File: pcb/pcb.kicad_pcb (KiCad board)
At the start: 4 copper layers, 88.3 x 88.4 mm, 32 parts, among them J1 USB_C_Receptacle_PowerOnly_6P, J10 Screw_Terminal_01x03, J2 Conn_01x04_Pin, J3 Screw_Terminal_01x03, J4 Screw_Terminal_01x04, J5 Screw_Terminal_01x02, J6 Screw_Terminal_01x02, J7 Screw_Terminal_01x04, J8 Screw_Terminal_01x07, J9 Screw_Terminal_01x02, K1 SANYOU_SRD_Form_A, Q1 2N2222A, Q2 AO3400A, U1 AMS1117-3.3, U2 ESP32-C6-MINI-1, U3 AM2302

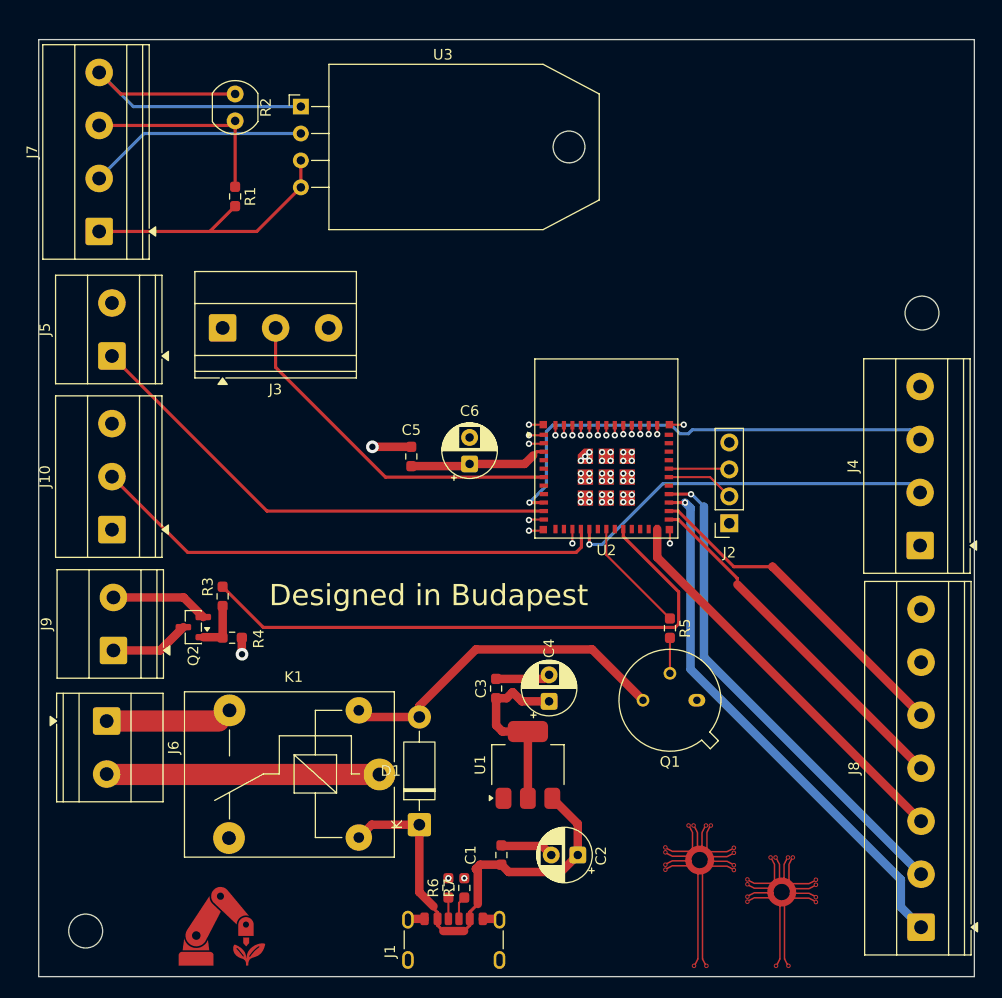
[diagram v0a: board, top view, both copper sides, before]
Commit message: fixing the layout
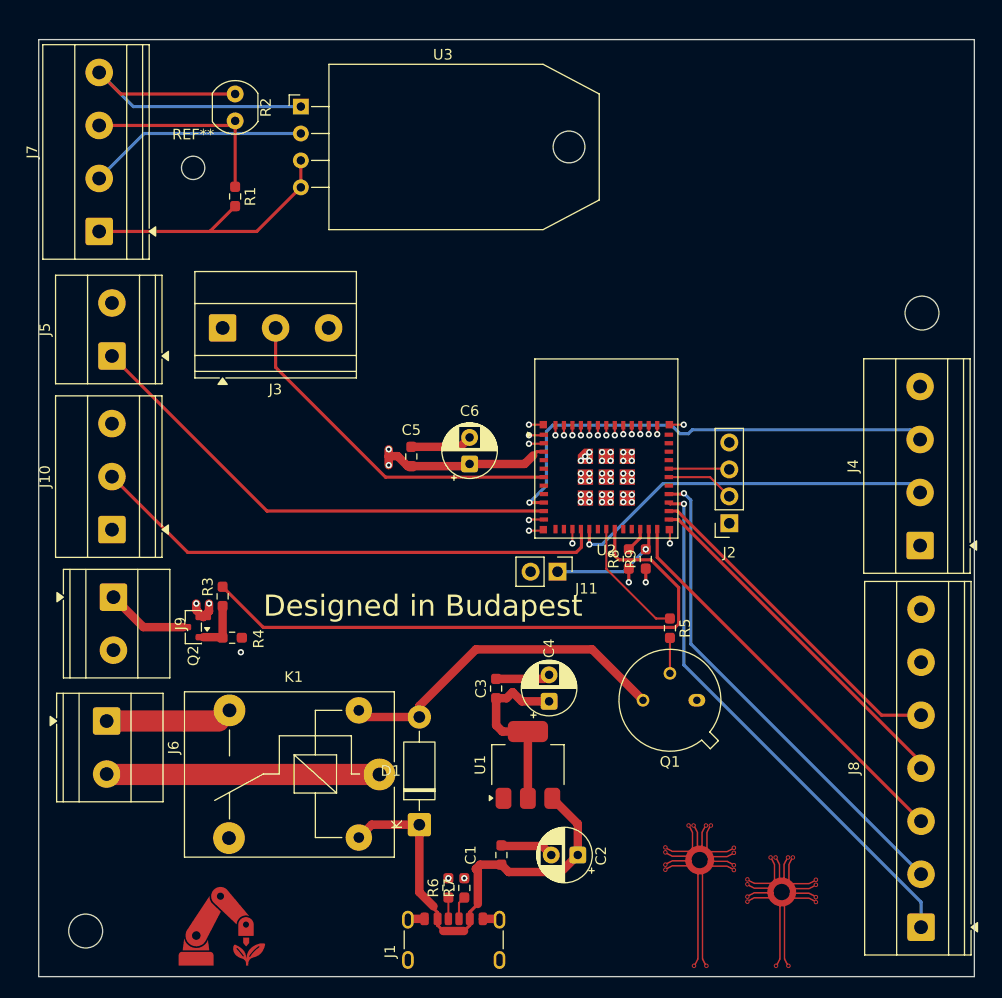
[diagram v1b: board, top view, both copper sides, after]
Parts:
- added J11: Conn_01x02_Pin, Connector_PinHeader_2.54mm:PinHeader_1x02_P2.54mm_Vertical, F.Cu at (113.4, 91.2)
- added R8: 10k, Resistor_SMD:R_0603_1608Metric_Pad0.98x0.95mm_HandSolder, F.Cu at (120.1, 90.0)
- added R9: 10k, Resistor_SMD:R_0603_1608Metric_Pad0.98x0.95mm_HandSolder, F.Cu at (121.7, 90.0)
- added REF**: MountingHole_2.2mm_M2, MountingHole:MountingHole_2.2mm_M2, F.Cu at (79.0, 53.1)
- moved J9 5.03 mm to (71.5, 93.6), turned to -90 degrees
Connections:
- U2 pad 19: unconnected-(U2-IO14-Pad19) -> /led_control/LED_control
- U2 pad 20: /led_control/LED_control -> unconnected-(U2-IO15-Pad20)
- U2 pad 22: unconnected-(U2-IO8-Pad22) -> /control/pullup for G8
- U2 pad 23: unconnected-(U2-IO9-Pad23) -> /control/input for G9
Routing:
- net /control/input for G9: track 0.00 -> 11.2 mm, vias 0 -> 1
- net +3.3V: track 31.0 -> 37.6 mm, vias 0 -> 4
- net GND: track 51.6 -> 46.6 mm, vias 61 -> 62
- net /screen/cs: track 49.3 -> 46.7 mm
- net /control/pullup for G8: track 0.00 -> 2.36 mm
- net /led_control/LED_control: track 55.9 -> 58.0 mm
- net /Pump control/PUMP_control: track 10.9 -> 11.7 mm

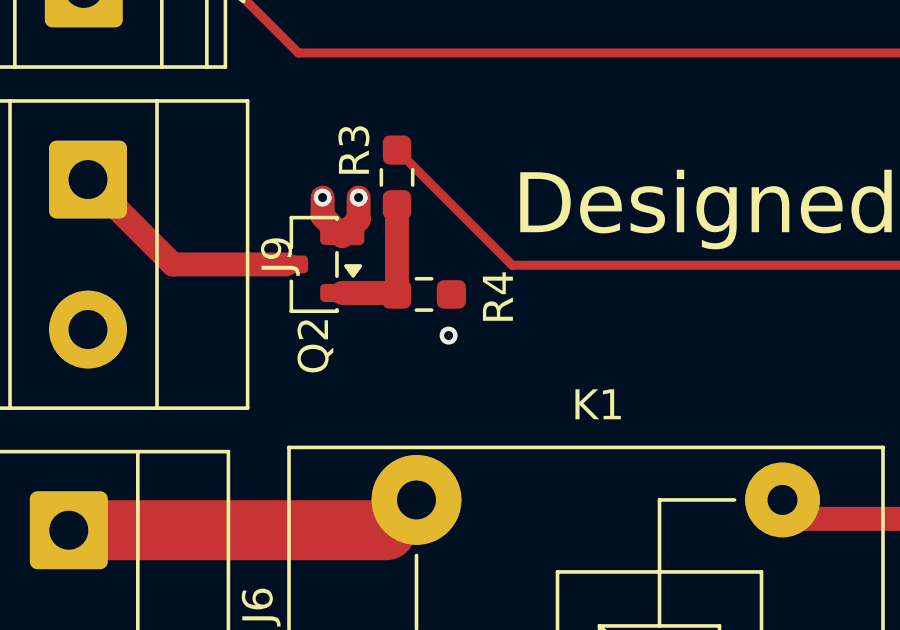
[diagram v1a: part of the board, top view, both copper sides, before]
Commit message: fixing the wireing mistake
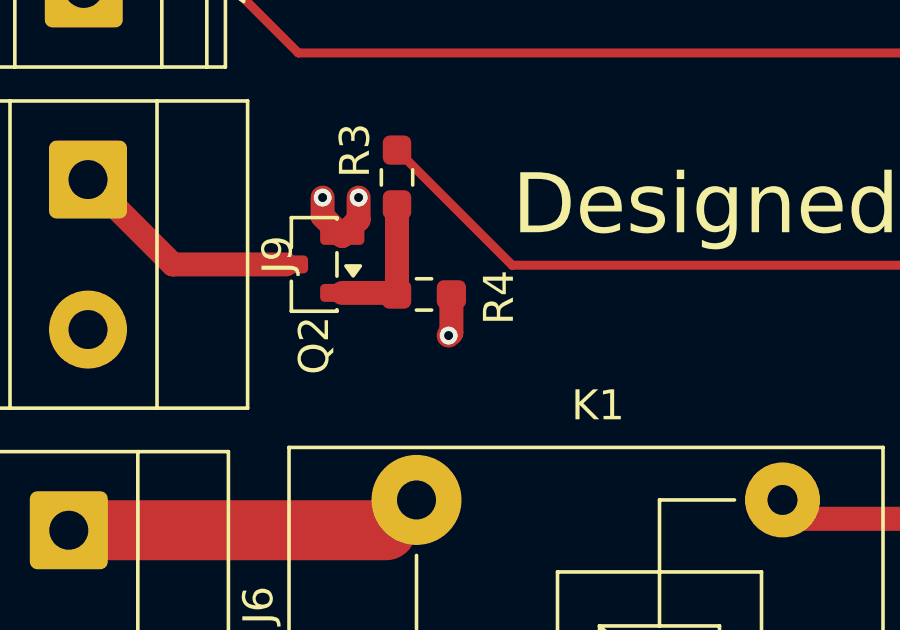
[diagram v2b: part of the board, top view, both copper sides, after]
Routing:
- net GND: track 46.6 -> 48.0 mm
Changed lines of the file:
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@@
+	)
+	(segment
+		(start 83.631932 98.7075)
+		(end 83.539432 98.8)
+		(width 0.8)
+		(layer "F.Cu")
+		(net 2)
+	)
+	(segment
+		(start 83.631932 97.429)
+		(end 83.631932 98.7075)
+		(width 0.8)
+		(layer "F.Cu")
+		(net 2)
 	)
 	(segment

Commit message: fixing pt.1
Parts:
- moved J3 9.92 mm to (91.7, 68.2), turned to 180 degrees
- moved J10 9.84 mm to (70.8, 77.4), turned to -90 degrees
- moved J5 4.78 mm to (70.8, 66.1), turned to -90 degrees
- moved J9 0.71 mm to (70.8, 93.8)
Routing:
- net /Sensor inputs/water level: track 46.8 -> 51.8 mm
- net Net-(J6-Pin_1): track 13.4 -> 12.0 mm
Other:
- board text added: "Soil tempature"
- board text added: "water level"

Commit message: Finding parts and folishing the pcb
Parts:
- C2, C4, C6: footprint Capacitor_THT:CP_Radial_D5.0mm_P2.50mm -> Capacitor_THT:CP_Radial_D5.0mm_P2.00mm
- moved J8 0.08 mm to (147.6, 124.7)
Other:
- board text added: "LED"
- board text added: "pump"

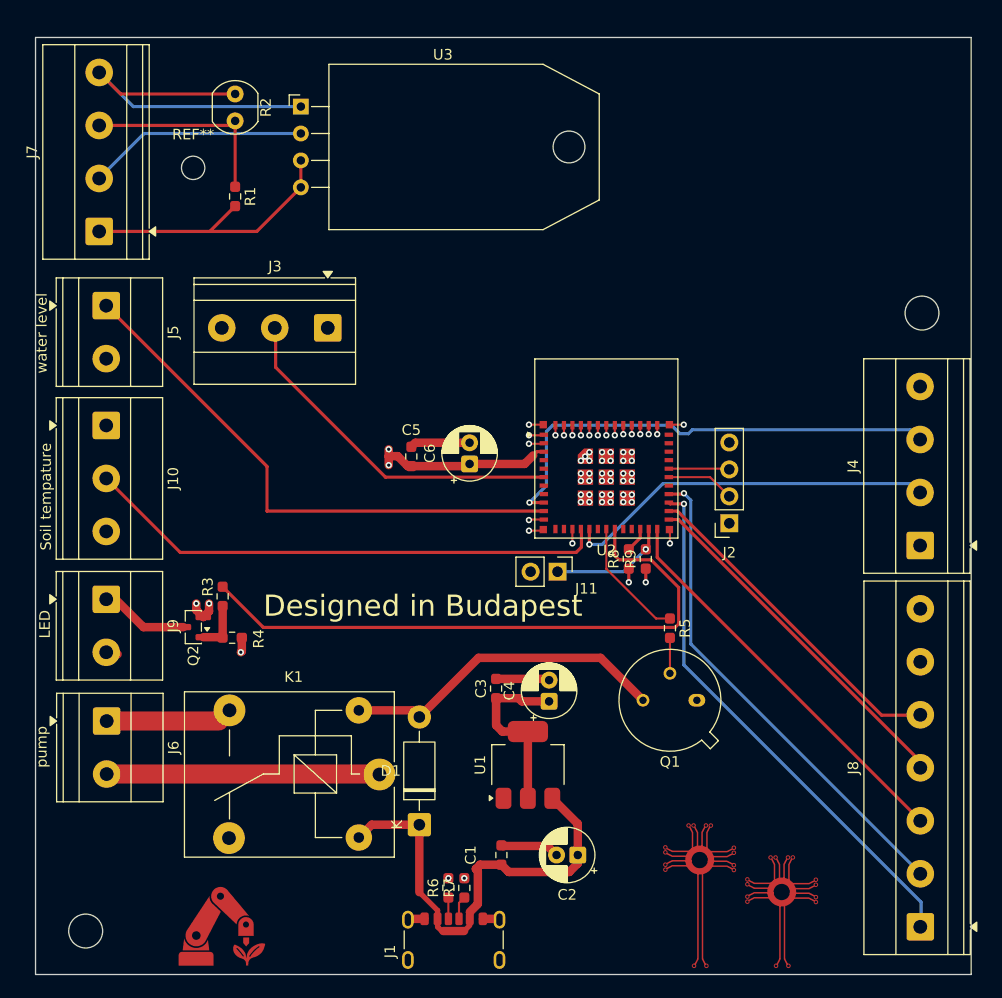
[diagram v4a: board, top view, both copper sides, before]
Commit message: cleaning the previus 3d model files and start designing the carrier for the main board
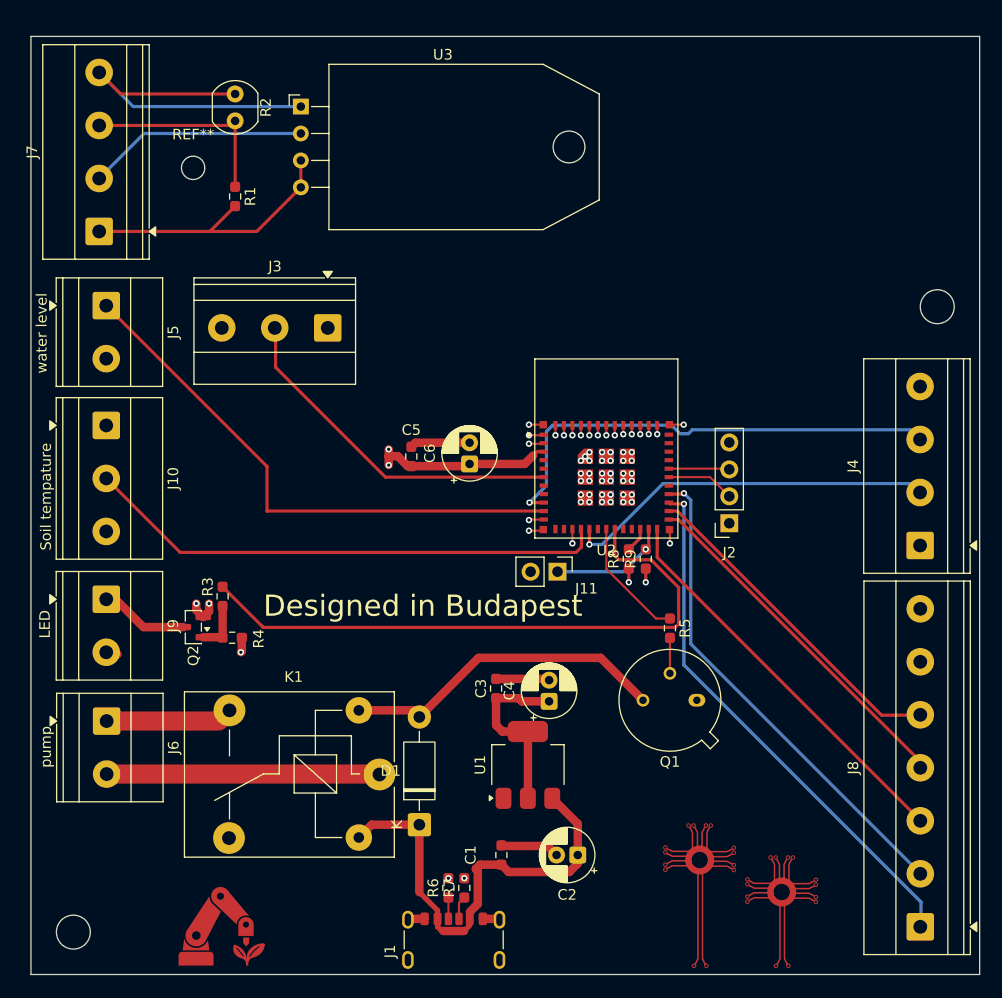
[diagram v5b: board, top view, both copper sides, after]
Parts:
- moved REF** 1.56 mm to (149.2, 66.2)
- moved REF** 1.16 mm to (67.7, 125.2)
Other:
- board size 88.3 x 88.4 mm -> 89.5 x 88.5 mm

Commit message: Finishing the usb-c module
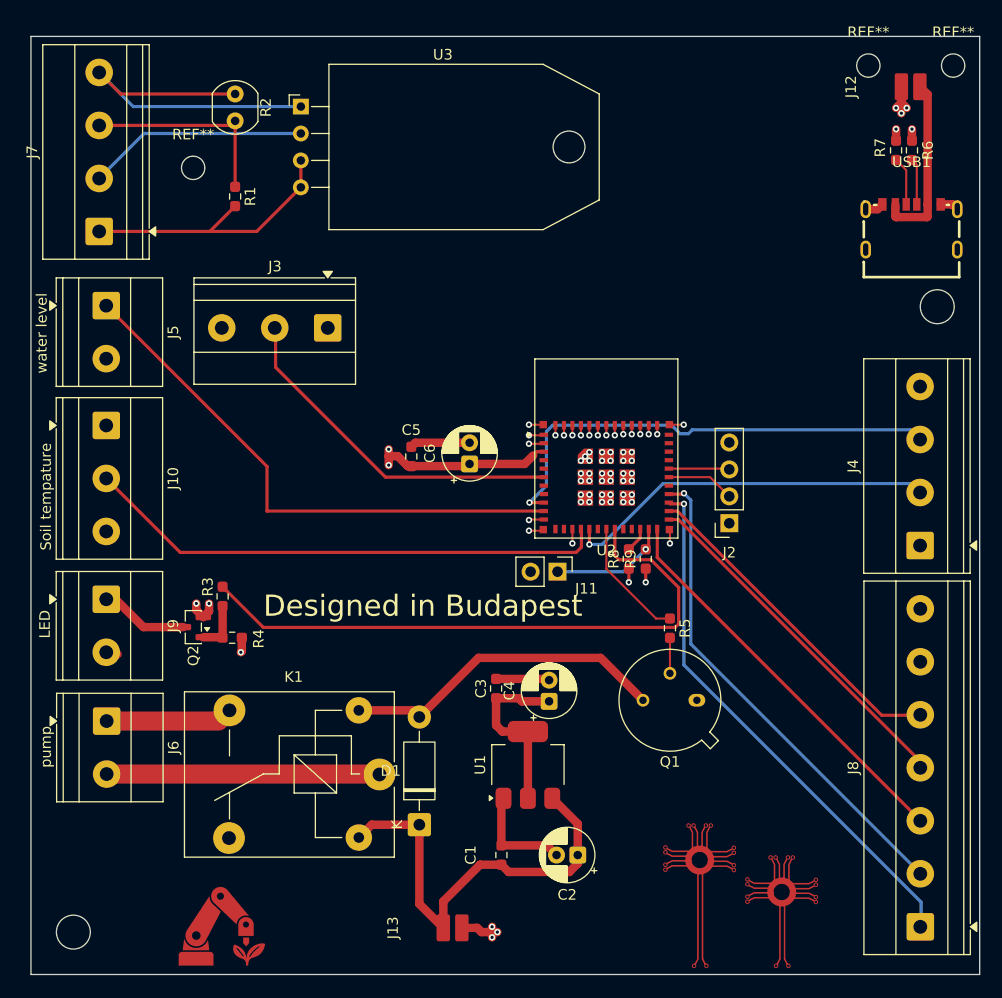
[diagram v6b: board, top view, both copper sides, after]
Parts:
- removed J1: USB_C_Receptacle_PowerOnly_6P, Connector_USB:USB_C_Receptacle_GCT_USB4125-xx-x_6P_TopMnt_Horizontal
- added J12: ~, Library:copper_pad 2x, F.Cu at (141.6, 45.5)
- added J13: ~, Library:copper_pad 2x, F.Cu at (98.4, 124.8)
- added REF**: MountingHole_2.2mm_M2, MountingHole:MountingHole_2.2mm_M2, F.Cu at (150.7, 43.5)
- added REF**: MountingHole_2.2mm_M2, MountingHole:MountingHole_2.2mm_M2, F.Cu at (142.7, 43.5)
- added USB1: TYPE-C 6P, lcsc_import:TYPE-C-SMD_TYPE-C-6P-073, F.Cu at (146.8, 58.7)
- moved R6 82.2 mm to (146.9, 51.5)
- moved R7 80.6 mm to (145.4, 51.5)
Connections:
- R6 pad 2: GND -> GND2
- R7 pad 2: GND -> GND2
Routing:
- net Net-(J12-Pad2): track 0.00 -> 16.8 mm
- net GND2: track 0.00 -> 9.60 mm, vias 0 -> 5
- net GND: track 48.2 -> 53.8 mm, vias 62 -> 63
- net Net-(USB1-CC1): track 2.21 -> 4.58 mm
- net Net-(USB1-CC2): track 2.01 -> 4.38 mm
- net +5V: track 43.2 -> 41.3 mm
- added copper zone on In1.Cu, net GND2

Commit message: Finishing the carrier board with the new usb-c modul
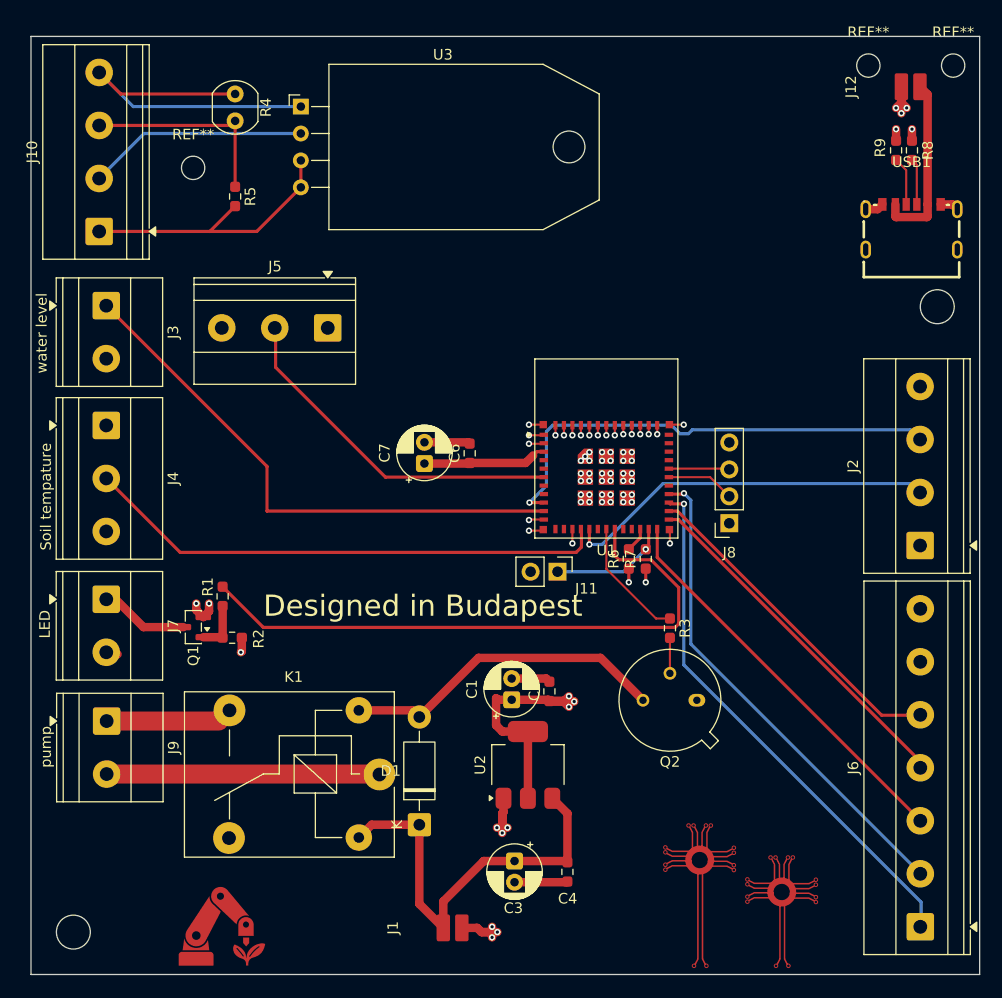
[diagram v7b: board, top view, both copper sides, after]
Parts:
- removed C5: 100nF, Resistor_SMD:R_0603_1608Metric_Pad0.98x0.95mm_HandSolder
- added C7: 10uF, Capacitor_THT:CP_Radial_D5.0mm_P2.00mm, F.Cu at (100.9, 81.0)
- C1, C3: value 100nF -> 10uF; footprint Resistor_SMD:R_0603_1608Metric_Pad0.98x0.95mm_HandSolder -> Capacitor_THT:CP_Radial_D5.0mm_P2.00mm
- C2, C4, C6: value 10uF -> 100nF; footprint Capacitor_THT:CP_Radial_D5.0mm_P2.00mm -> Resistor_SMD:R_0603_1608Metric_Pad0.98x0.95mm_HandSolder
- moved C3 16.4 mm to (109.4, 118.5), turned to -90 degrees
- moved C4 16.2 mm to (114.3, 119.5), turned to -90 degrees
- moved C2 15.7 mm to (112.6, 102.5), turned to 90 degrees
- moved C1 14.7 mm to (109.1, 103.3)
- moved C6 1.00 mm to (105.1, 80.0)
- renumbered J13 to J1, J7 to J10, J4 to J2, J5 to J3, J10 to J4, J3 to J5, J8 to J6, J9 to J7, J2 to J8, J6 to J9, Q2 to Q1, Q1 to Q2, R3 to R1, R4 to R2, R5 to R3, R2 to R4, R1 to R5, R8 to R6, R9 to R7, R6 to R8, R7 to R9, U2 to U1, U1 to U2
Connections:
- C1 pad 1: +5V -> +3.3V
- C2 pad 1: +5V -> +3.3V
- C3 pad 1: +3.3V -> +5V
- C4 pad 1: +3.3V -> +5V
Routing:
- net +5V: track 41.3 -> 39.3 mm
- net GND: track 53.8 -> 52.0 mm, vias 63 -> 66
- net +3.3V: track 37.2 -> 38.3 mm, vias 4 -> 5
